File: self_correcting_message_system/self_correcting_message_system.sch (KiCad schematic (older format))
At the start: 34 parts, among them U01 plot_v1, U02 plot_v1, U03 plot_v1, U101 adc_bridge_1, U102 vinayak_inverter, U103 vinayak_inverter, U104 dac_bridge_1, U105 plot_v1, U106 adc_bridge_1, U107 vinayak_inverter, U108 vinayak_inverter, U109 dac_bridge_1, U110 plot_v1, U201 adc_bridge_2, U202 d_xnor, U203 dac_bridge_1, U204 plot_v1, X01 avsd_opamp, X02 avsd_opamp

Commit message: Window Comparitor
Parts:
- removed U?: vinayak_hamming_ecoder, symbol vinayak_hamming_ecoder
- removed U? (x2): adc_bridge_8, symbol adc_bridge_8
- removed U?: vinayak_mux, symbol vinayak_mux
- removed U?: plot_v1, symbol plot_v1
- removed U?: adc_bridge_2, symbol adc_bridge_2
- removed U?: vinayak_mod16, symbol vinayak_mod16
- removed U?: dac_bridge_4, symbol dac_bridge_4
- removed v?: sine, R1, symbol sine
- added U04, U05: plot_v1, symbol plot_v1
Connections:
- net labels added: In1, In2
- wire segments 80 -> 60
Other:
- moved on the sheet: U201, U202, U203, U204

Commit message: Frequency Divider
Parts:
- added U301: adc_bridge_1, symbol adc_bridge_1
- added U302: vinayak_frequency_divider, symbol vinayak_frequency_divider
- added U303: dac_bridge_1, symbol dac_bridge_1
- added U304, U305: plot_v1, symbol plot_v1
- added v303: sine, R1, symbol sine
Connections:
- net GND: now also v303.2 (-)
- new net: U301.2 (OUT1), U302.1 (clk0)
- new net: U302.2 (out_clk0), U303.1 (IN1)
- new net frepOUT: U303.2 (OUT1), U305.~
- new net freqIn: U301.1 (IN1), U304.~, v303.1 (+)
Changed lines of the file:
@@
 Text GLabel -14000 -850 0    60   Input ~ 0
 In2
-Wire Wire Line
-	-15200 1150 -15200 -3150
-Wire Wire Line
-	-15200 -3150 -14800 -3150
-Wire Wire Line
-	-14800 -1600 -15200 -1600
-Connection ~ -15200 -1600
-Wire Wire Line
-	-14800 100  -15200 100
-Connection ~ -15200 100
-Wire Wire Line
-	-14600 400  -14600 750
-Wire Wire Line
-	-14600 750  -15200 750
-Connection ~ -15200 750
-Wire Wire Line
-	-14600 -200 -14600 -1300
-Wire Wire Line
-	-14600 -1900 -14600 -2850
-Wire Wire Line
-	-18550 650  -18550 450
-Wire Wire Line
-	-13050 -2300 -18550 -2300
-Wire Wire Line
-	-18550 -2300 -18550 -450
-Wire Wire Line
-	-18800 -1050 -18550 -1050
-Connection ~ -18550 -1050
-Wire Wire Line
-	-13100 -900 -13500 -900
-Wire Wire Line
-	-13500 -900 -13500 -2300
-Connection ~ -13500 -2300
-Wire Wire Line
-	-13100 -700 -14600 -700
-Connection ~ -14600 -700
-Wire Wire Line
-	-13050 -2500 -14600 -2500
-Connection ~ -14600 -2500
-Wire Wire Line
-	-17750 -2850 -12450 -2850
-Wire Wire Line
-	-17750 -3600 -17750 -450
-Wire Wire Line
-	-12500 -1250 -12500 -1400
-Wire Wire Line
-	-12500 -1400 -13350 -1400
-Wire Wire Line
-	-13350 -1400 -13350 -2850
-Connection ~ -13350 -2850
-Wire Wire Line
-	-12450 -1950 -17000 -1950
-Wire Wire Line
-	-17000 -1950 -17000 -450
-Wire Wire Line
-	-12500 -350 -13150 -350
-Wire Wire Line
-	-13150 -350 -13150 -1950
-Connection ~ -13150 -1950
-Wire Wire Line
-	-17000 650  -17000 450
-Wire Wire Line
-	-17750 650  -17750 450
-Wire Wire Line
-	-12200 -1950 -12200 -1700
-Wire Wire Line
-	-12200 -1700 -11650 -1700
-Wire Wire Line
-	-11650 -1700 -11650 150
-Wire Wire Line
-	-11650 150  -13150 150
-Wire Wire Line
-	-13150 150  -13150 750
-Wire Wire Line
-	-12250 -350 -12250 150
-Connection ~ -12250 150
-Wire Wire Line
-	-11800 -850 -11400 -850
-Wire Wire Line
-	-11400 -850 -11400 -1000
-Wire Wire Line
-	-11750 -2450 -11450 -2450
-Wire Wire Line
-	-11450 -2450 -11450 -2700
-Wire Wire Line
-	-14600 -3450 -14600 -3600
-Wire Wire Line
-	-14600 -3600 -17750 -3600
-Connection ~ -17750 -2850
-Wire Wire Line
-	-18350 1700 -19100 1700
-Wire Wire Line
-	-17200 1700 -16450 1700
-Wire Wire Line
-	-15050 1700 -14300 1700
-Wire Wire Line
-	-12900 1700 -12300 1700
-Wire Wire Line
-	-11150 1700 -10200 1700
-Wire Wire Line
-	-10200 1700 -10200 1350
-Wire Wire Line
-	-18350 3100 -19100 3100
-Wire Wire Line
-	-17200 3100 -16450 3100
-Wire Wire Line
-	-15050 3100 -14300 3100
-Wire Wire Line
-	-12900 3100 -12300 3100
-Wire Wire Line
-	-11150 3100 -10200 3100
-Wire Wire Line
-	-10200 3100 -10200 2750
-Wire Wire Line
-	-12700 4900 -12050 4900
-Wire Wire Line
-	-17850 4850 -18150 4850
-Wire Wire Line
-	-17850 4950 -18150 4950
-Wire Wire Line
-	-12050 4900 -12050 4550
-Wire Wire Line
-	-14000 -2650 -14000 -2500
-Connection ~ -14000 -2500
-Wire Wire Line
-	-14000 -950 -14000 -700
-Connection ~ -14000 -700
-Wire Wire Line
-	-15750 4950 -16700 4950
-Wire Wire Line
-	-16700 4850 -15750 4850
-Wire Wire Line
-	-13850 4900 -14850 4900
 $Comp
 L d_xnor U202
@@
 	1    0    0    -1
 $EndComp
+$Comp
+L adc_bridge_1 U301
+U 1 1 634274D1
+P -6850 -2450
+F 0 "U301" H -6850 -2450 60  0000 C CNN
+F 1 "adc_bridge_1" H -6850 -2300 60  0000 C CNN
+F 2 "" H -6850 -2450 60  0000 C CNN
+F 3 "" H -6850 -2450 60  0000 C CNN
+	1    -6850 -2450
+	1    0    0    -1
+$EndComp
+$Comp
+L vinayak_frequency_divider U302
+U 1 1 63427562
+P -8050 -600
+F 0 "U302" H -5200 1200 60  0000 C CNN
+F 1 "vinayak_frequency_divider" H -5200 1400 60  0000 C CNN
+F 2 "" H -5200 1350 60  0000 C CNN
+F 3 "" H -5200 1350 60  0000 C CNN
+	1    -8050 -600
+	1    0    0    -1
+$EndComp
+$Comp
+L dac_bridge_1 U303
+U 1 1 63427679
+P -3650 -2450
+F 0 "U303" H -3650 -2450 60  0000 C CNN
+F 1 "dac_bridge_1" H -3650 -2300 60  0000 C CNN
+F 2 "" H -3650 -2450 60  0000 C CNN
+F 3 "" H -3650 -2450 60  0000 C CNN
+	1    -3650 -2450
+	1    0    0    -1
+$EndComp
+$Comp
+L plot_v1 U305
+U 1 1 6342ABC3
+P -2900 -2850
+F 0 "U305" H -2900 -2350 60  0000 C CNN
+F 1 "plot_v1" H -2700 -2500 60  0000 C CNN
+F 2 "" H -2900 -2850 60  0000 C CNN
+F 3 "" H -2900 -2850 60  0000 C CNN
+	1    -2900 -2850
+	1    0    0    -1
+$EndComp
+$Comp
+L plot_v1 U304
+U 1 1 6342AC54
+P -7500 -2750
+F 0 "U304" H -7500 -2250 60  0000 C CNN
+F 1 "plot_v1" H -7300 -2400 60  0000 C CNN
+F 2 "" H -7500 -2750 60  0000 C CNN
+F 3 "" H -7500 -2750 60  0000 C CNN
+	1    -7500 -2750
+	1    0    0    -1
+$EndComp
+Text GLabel -7500 -2850 2    60   Input ~ 0
+freqIn
+Text GLabel -2900 -2950 0    60   Output ~ 0
+frepOUT
+Connection ~ -7500 -2500
+Wire Wire Line
+	-7500 -2950 -7500 -2500
+Wire Wire Line
+	-2900 -2500 -2900 -3050
+Wire Wire Line
+	-3100 -2500 -2900 -2500
+Wire Wire Line
+	-7800 -2500 -7450 -2500
+Wire Wire Line
+	-4500 -2500 -4250 -2500
+Wire Wire Line
+	-6300 -2500 -5900 -2500
+Wire Wire Line
+	-13850 4900 -14850 4900
+Wire Wire Line
+	-16700 4850 -15750 4850
+Wire Wire Line
+	-15750 4950 -16700 4950
+Connection ~ -14000 -700
+Wire Wire Line
+	-14000 -950 -14000 -700
+Connection ~ -14000 -2500
+Wire Wire Line
+	-14000 -2650 -14000 -2500
+Wire Wire Line
+	-12050 4900 -12050 4550
+Wire Wire Line
+	-17850 4950 -18150 4950
+Wire Wire Line
+	-17850 4850 -18150 4850
+Wire Wire Line
+	-12700 4900 -12050 4900
+Wire Wire Line
+	-10200 3100 -10200 2750
+Wire Wire Line
+	-11150 3100 -10200 3100
+Wire Wire Line
+	-12900 3100 -12300 3100
+Wire Wire Line
+	-15050 3100 -14300 3100
+Wire Wire Line
+	-17200 3100 -16450 3100
+Wire Wire Line
+	-18350 3100 -19100 3100
+Wire Wire Line
+	-10200 1700 -10200 1350
+Wire Wire Line
+	-11150 1700 -10200 1700
+Wire Wire Line
+	-12900 1700 -12300 1700
+Wire Wire Line
+	-15050 1700 -14300 1700
+Wire Wire Line
+	-17200 1700 -16450 1700
+Wire Wire Line
+	-18350 1700 -19100 1700
+Connection ~ -17750 -2850
+Wire Wire Line
+	-14600 -3600 -17750 -3600
+Wire Wire Line
+	-14600 -3450 -14600 -3600
+Wire Wire Line
+	-11450 -2450 -11450 -2700
+Wire Wire Line
+	-11750 -2450 -11450 -2450
+Wire Wire Line
+	-11400 -850 -11400 -1000
+Wire Wire Line
+	-11800 -850 -11400 -850
+Connection ~ -12250 150
+Wire Wire Line
+	-12250 -350 -12250 150
+Wire Wire Line
+	-13150 150  -13150 750
+Wire Wire Line
+	-11650 150  -13150 150
+Wire Wire Line
+	-11650 -1700 -11650 150
+Wire Wire Line
+	-12200 -1700 -11650 -1700
+Wire Wire Line
+	-12200 -1950 -12200 -1700
+Wire Wire Line
+	-17750 650  -17750 450
+Wire Wire Line
+	-17000 650  -17000 450
+Connection ~ -13150 -1950
+Wire Wire Line
+	-13150 -350 -13150 -1950
+Wire Wire Line
+	-12500 -350 -13150 -350
+Wire Wire Line
+	-17000 -1950 -17000 -450
+Wire Wire Line
+	-12450 -1950 -17000 -1950
+Connection ~ -13350 -2850
+Wire Wire Line
+	-13350 -1400 -13350 -2850
+Wire Wire Line
+	-12500 -1400 -13350 -1400
+Wire Wire Line
+	-12500 -1250 -12500 -1400
+Wire Wire Line
+	-17750 -3600 -17750 -450
+Wire Wire Line
+	-17750 -2850 -12450 -2850
+Connection ~ -14600 -2500
+Wire Wire Line
+	-13050 -2500 -14600 -2500
+Connection ~ -14600 -700
+Wire Wire Line
+	-13100 -700 -14600 -700
+Connection ~ -13500 -2300
+Wire Wire Line
+	-13500 -900 -13500 -2300
+Wire Wire Line
+	-13100 -900 -13500 -900
+Connection ~ -18550 -1050
+Wire Wire Line
+	-18800 -1050 -18550 -1050
+Wire Wire Line
+	-18550 -2300 -18550 -450
+Wire Wire Line
+	-13050 -2300 -18550 -2300
+Wire Wire Line
+	-18550 650  -18550 450
+Wire Wire Line
+	-14600 -1900 -14600 -2850
+Wire Wire Line
+	-14600 -200 -14600 -1300
+Connection ~ -15200 750
+Wire Wire Line
+	-14600 750  -15200 750
+Wire Wire Line
+	-14600 400  -14600 750
+Connection ~ -15200 100
+Wire Wire Line
+	-14800 100  -15200 100
+Connection ~ -15200 -1600
+Wire Wire Line
+	-14800 -1600 -15200 -1600
+Wire Wire Line
+	-15200 -3150 -14800 -3150
+Wire Wire Line
+	-15200 1150 -15200 -3150
+$Comp
+L eSim_GND #PWR06
+U 1 1 6342EA90
+P -7800 -1600
+F 0 "#PWR06" H -7800 -1850 50  0001 C CNN
+F 1 "eSim_GND" H -7800 -1750 50  0000 C CNN
+F 2 "" H -7800 -1600 50  0001 C CNN
+F 3 "" H -7800 -1600 50  0001 C CNN
+	1    -7800 -1600
+	1    0    0    -1
+$EndComp
+$Comp
+L sine v303
+U 1 1 6342E9B9
+P -7800 -2050
+F 0 "v303" H -8000 -1950 60  0000 C CNN
+F 1 "sine" H -8000 -2100 60  0000 C CNN
+F 2 "R1" H -8100 -2050 60  0000 C CNN
+F 3 "" H -7800 -2050 60  0000 C CNN
+	1    -7800 -2050
+	1    0    0    -1
+$EndComp
+Wire Notes Line
+	-9150 -4950 -9150 6300
+Wire Notes Line
+	-9150 6300 -20250 6300
+Wire Notes Line
+	-20250 6300 -20250 -4950
+Wire Notes Line
+	-20250 -4950 -9150 -4950
 $EndSCHEMATC

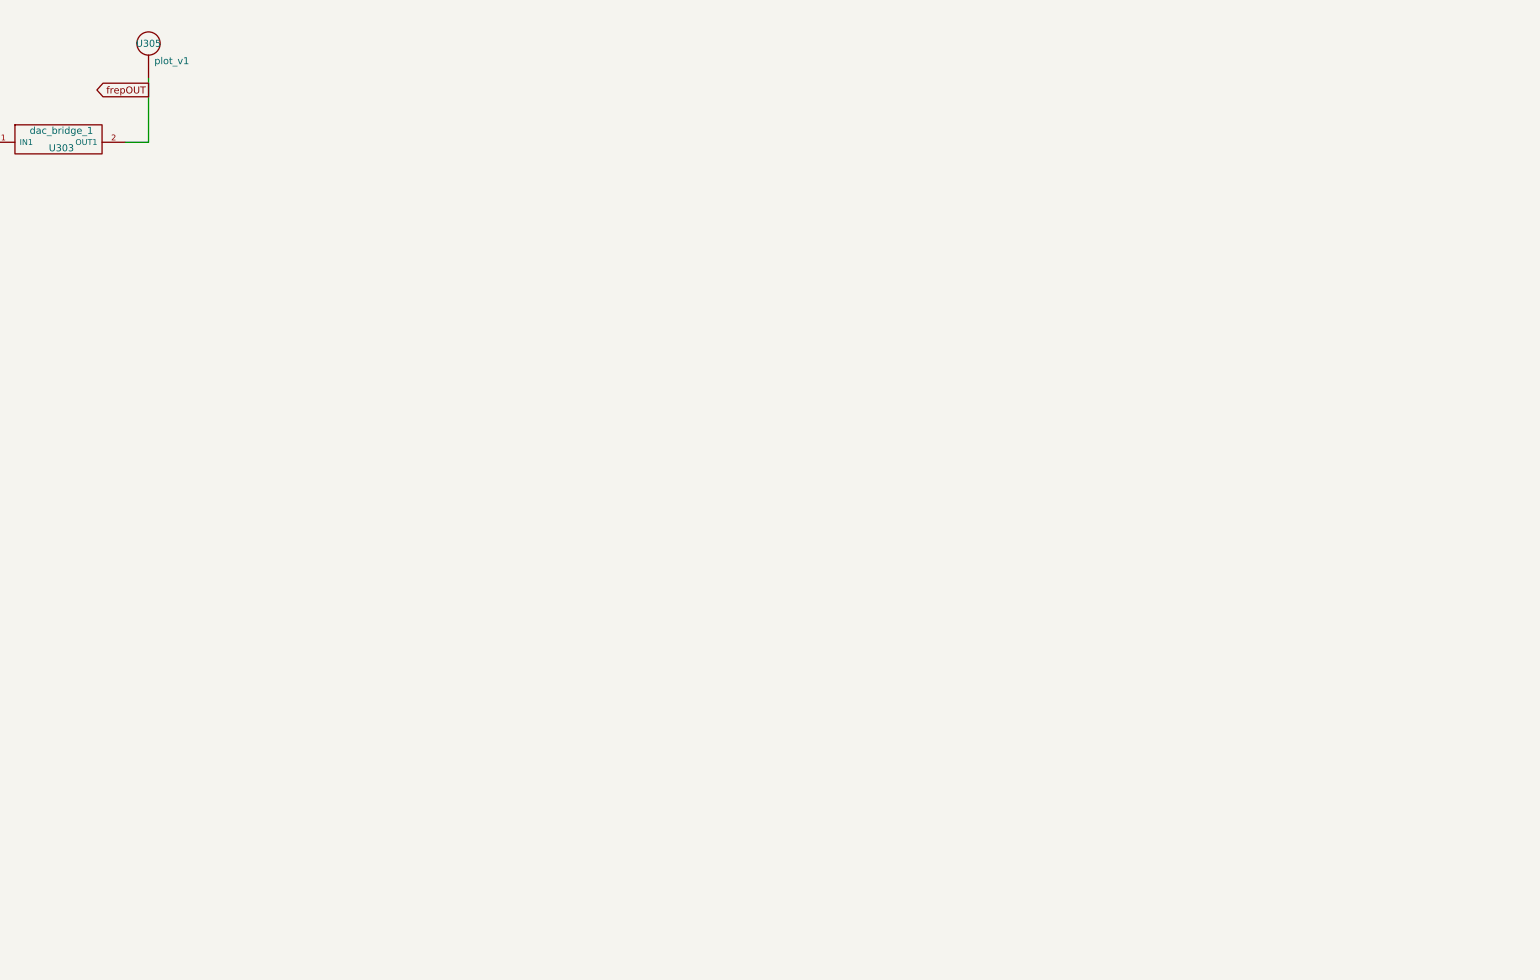
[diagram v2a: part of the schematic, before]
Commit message: Hamming Encoder
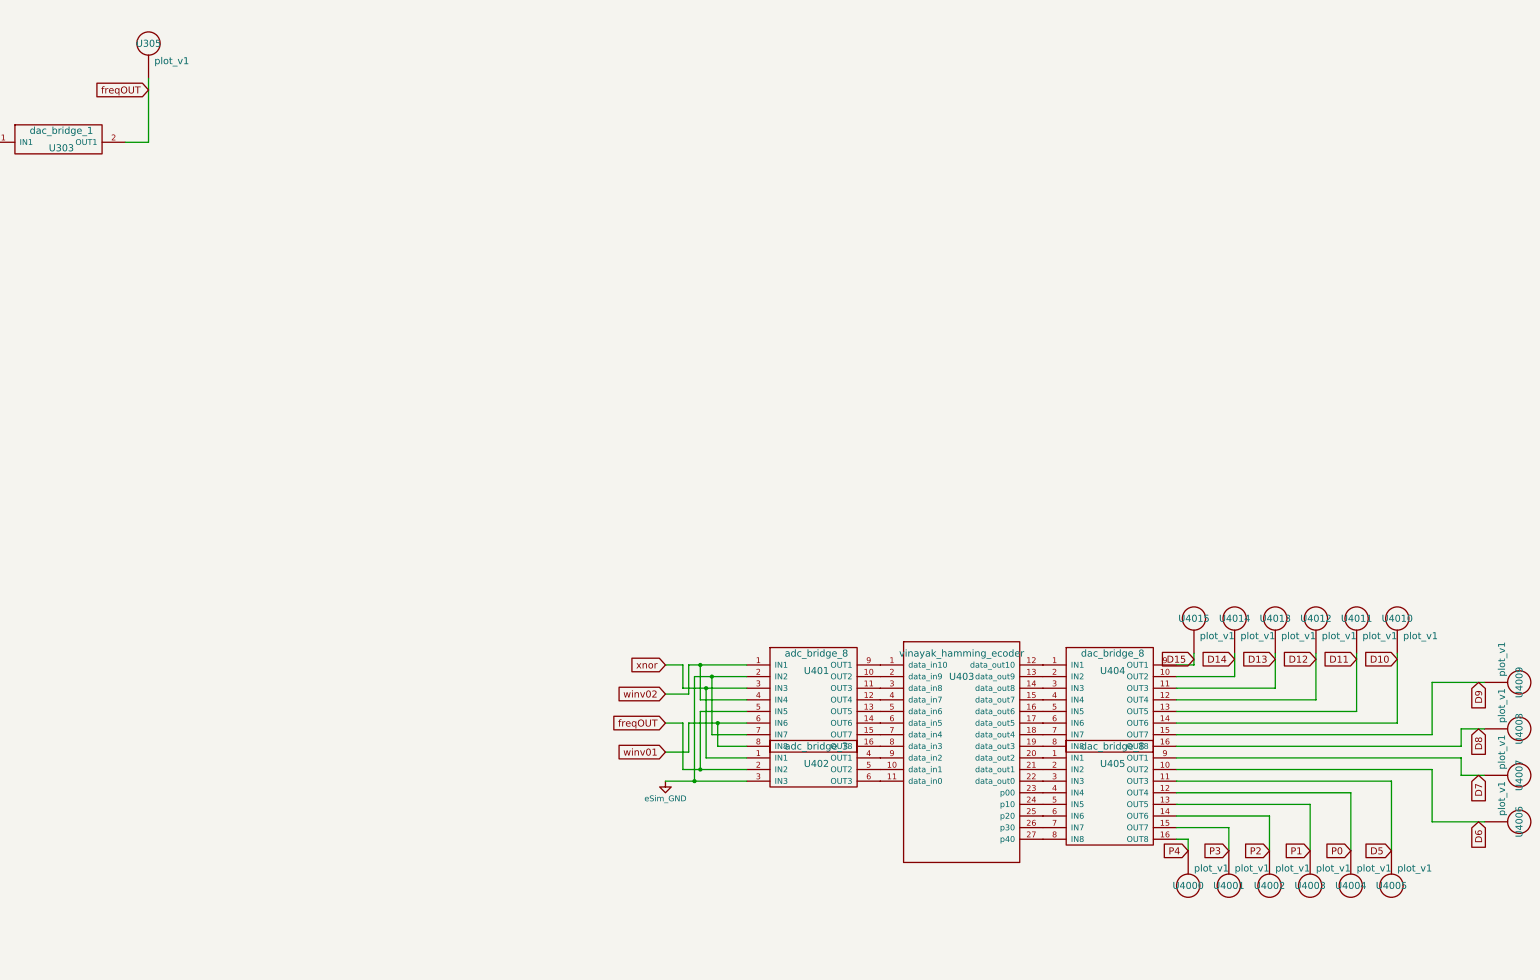
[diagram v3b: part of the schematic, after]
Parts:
- added U4000, U4001, U4002, U4003, U4004, U4005, U4006, U4007, U4008, U4009, U4010, U4011, U4012, U4013, U4014, U4015: plot_v1, symbol plot_v1
- added U401: adc_bridge_8, symbol adc_bridge_8
- added U402: adc_bridge_3, symbol adc_bridge_3
- added U403: vinayak_hamming_ecoder, symbol vinayak_hamming_ecoder
- added U404, U405: dac_bridge_8, symbol dac_bridge_8
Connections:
- net GND: now also U401.2 (IN2), U401.7 (IN7), U402.3 (IN3)
- net winv01: now also U401.6 (IN6), U401.8 (IN8)
- net winv02: now also U401.1 (IN1), U401.4 (IN4)
- net frepOUT renamed freqOUT
- net freqOUT: now also U401.5 (IN5), U402.2 (IN2)
- new net: U401.9 (OUT1), U403.1 (data_in10)
- new net: U402.5 (OUT2), U403.10 (data_in1)
- new net: U402.6 (OUT3), U403.11 (data_in0)
- new net: U403.12 (data_out10), U404.1 (IN1)
- new net: U403.13 (data_out9), U404.2 (IN2)
- new net: U403.14 (data_out8), U404.3 (IN3)
- new net: U403.15 (data_out7), U404.4 (IN4)
- new net: U403.16 (data_out6), U404.5 (IN5)
- new net: U403.17 (data_out5), U404.6 (IN6)
- new net: U403.18 (data_out4), U404.7 (IN7)
- new net: U403.19 (data_out3), U404.8 (IN8)
- new net: U401.10 (OUT2), U403.2 (data_in9)
- new net: U403.20 (data_out2), U405.1 (IN1)
- new net: U403.21 (data_out1), U405.2 (IN2)
- new net: U403.22 (data_out0), U405.3 (IN3)
- new net: U403.23 (p00), U405.4 (IN4)
- new net: U403.24 (p10), U405.5 (IN5)
- new net: U403.25 (p20), U405.6 (IN6)
- new net: U403.26 (p30), U405.7 (IN7)
- new net: U403.27 (p40), U405.8 (IN8)
- new net: U401.11 (OUT3), U403.3 (data_in8)
- new net: U401.12 (OUT4), U403.4 (data_in7)
- new net: U401.13 (OUT5), U403.5 (data_in6)
- new net: U401.14 (OUT6), U403.6 (data_in5)
- new net: U401.15 (OUT7), U403.7 (data_in4)
- new net: U401.16 (OUT8), U403.8 (data_in3)
- new net: U402.4 (OUT1), U403.9 (data_in2)
- new net D10: U4010.~, U404.14 (OUT6)
- new net D11: U4011.~, U404.13 (OUT5)
- new net D12: U4012.~, U404.12 (OUT4)
- new net D13: U4013.~, U404.11 (OUT3)
- new net D14: U4014.~, U404.10 (OUT2)
- new net D15: U4015.~, U404.9 (OUT1)
- new net D5: U4005.~, U405.11 (OUT3)
- new net D6: U4006.~, U405.10 (OUT2)
- new net D7: U4007.~, U405.9 (OUT1)
- new net D8: U4008.~, U404.16 (OUT8)
- new net D9: U4009.~, U404.15 (OUT7)
- new net P0: U4004.~, U405.12 (OUT4)
- new net P1: U4003.~, U405.13 (OUT5)
- new net P2: U4002.~, U405.14 (OUT6)
- new net P3: U4001.~, U405.15 (OUT7)
- new net P4: U4000.~, U405.16 (OUT8)
- new net xnor: U401.3 (IN3), U402.1 (IN1)

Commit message: Self Correcting Message System
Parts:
- added U502, U606, U607, U608, U609, U610, U611, U612, U613, U614, U615, U616, U617, U618, U619, U620, U621: plot_v1, symbol plot_v1
- added U601, U602: adc_bridge_8, symbol adc_bridge_8
- added U603: vinayak_hamming_decoder, symbol vinayak_hamming_decoder
- added U604, U605: dac_bridge_8, symbol dac_bridge_8
- added v501: pulse, R1, symbol pulse
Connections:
- net D10: now also U601.6 (IN6)
- net D11: now also U601.5 (IN5)
- net D12: now also U601.4 (IN4)
- net D13: now also U601.3 (IN3)
- net D14: now also U601.2 (IN2)
- net D15: now also U601.1 (IN1)
- net D5: now also U602.5 (IN5)
- net D6: now also U602.3 (IN3)
- net D7: now also U602.2 (IN2)
- net D8: now also U602.1 (IN1)
- net D9: now also U601.7 (IN7)
- net GND: now also v501.2 (-); no longer U401.7 (IN7)
- net P0: now also U602.8 (IN8)
- net P1: now also U602.7 (IN7)
- net P2: now also U602.6 (IN6)
- net P3: now also U602.4 (IN4)
- net P4: now also U601.8 (IN8)
- new net: U601.9 (OUT1), U603.1 (data_in15)
- new net: U602.10 (OUT2), U603.10 (data_in6)
- new net: U602.11 (OUT3), U603.11 (data_in5)
- new net: U602.12 (OUT4), U603.12 (data_in4)
- new net: U602.13 (OUT5), U603.13 (data_in3)
- new net: U602.14 (OUT6), U603.14 (data_in2)
- new net: U602.15 (OUT7), U603.15 (data_in1)
- new net: U602.16 (OUT8), U603.16 (data_in0)
- new net: U603.17 (parity0), U604.1 (IN1)
- new net: U603.18 (p3), U604.2 (IN2)
- new net: U603.19 (p2), U604.3 (IN3)
- new net: U601.10 (OUT2), U603.2 (data_in14)
- new net: U603.20 (p1), U604.4 (IN4)
- new net: U603.21 (p0), U604.5 (IN5)
- new net: U603.22 (data10), U604.6 (IN6)
- new net: U603.23 (data9), U604.7 (IN7)
- new net: U603.24 (data8), U604.8 (IN8)
- new net: U603.25 (data7), U605.1 (IN1)
- new net: U603.26 (data6), U605.2 (IN2)
- new net: U603.27 (data5), U605.3 (IN3)
- new net: U603.28 (data4), U605.4 (IN4)
- new net: U603.29 (data3), U605.5 (IN5)
- new net: U601.11 (OUT3), U603.3 (data_in13)
- new net: U603.30 (data2), U605.6 (IN6)
- new net: U603.31 (data1), U605.7 (IN7)
- new net: U603.32 (data0), U605.8 (IN8)
- new net: U601.12 (OUT4), U603.4 (data_in12)
- new net: U601.13 (OUT5), U603.5 (data_in11)
- new net: U601.14 (OUT6), U603.6 (data_in10)
- new net: U601.15 (OUT7), U603.7 (data_in9)
- new net: U601.16 (OUT8), U603.8 (data_in8)
- new net: U602.9 (OUT1), U603.9 (data_in7)
- new net CD0: U605.16 (OUT8), U606.~
- new net CD1: U605.15 (OUT7), U607.~
- new net CD10: U604.14 (OUT6), U616.~
- new net CD2: U605.14 (OUT6), U608.~
- new net CD3: U605.13 (OUT5), U609.~
- new net CD4: U605.12 (OUT4), U610.~
- new net CD5: U605.11 (OUT3), U611.~
- new net CD6: U605.10 (OUT2), U612.~
- new net CD7: U605.9 (OUT1), U613.~
- new net CD8: U604.16 (OUT8), U614.~
- new net CD9: U604.15 (OUT7), U615.~
- new net clk: U401.7 (IN7), U502.~, v501.1 (+)
- new net pari0: U604.13 (OUT5), U617.~
- new net pari1: U604.12 (OUT4), U618.~
- new net pari2: U604.11 (OUT3), U619.~
- new net pari3: U604.10 (OUT2), U620.~
- new net parity0: U604.9 (OUT1), U621.~
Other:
- moved on the sheet: SC01, SC02, SC03, U01, U02, U03, U04, U05, U101, U102, U103, U104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

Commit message: Images : Self Correcting Message System
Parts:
- removed U202: d_xnor, symbol d_xnor
- added SC202: sky130_stdcells__xnor2_1, symbol sky130_stdcells__xnor2_1
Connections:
- net at U201.3 (OUT1): now also SC202.1 (A)
- net at U201.4 (OUT2): now also SC202.2 (B)
- net at U203.1 (IN1): now also SC202.3 (Y)
